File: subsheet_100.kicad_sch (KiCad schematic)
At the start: 21 parts, among them U100 MC68000_PLCC_68_PHY, U100_DIP64 MC68000_DIP_64_SOCKET

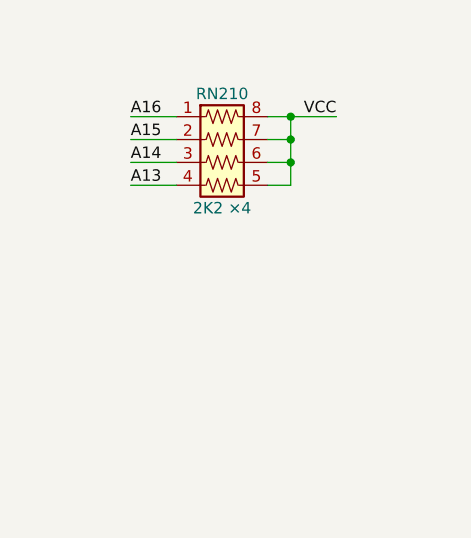
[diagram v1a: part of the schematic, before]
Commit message: add gnd/vcc symbol to start replacing local labels
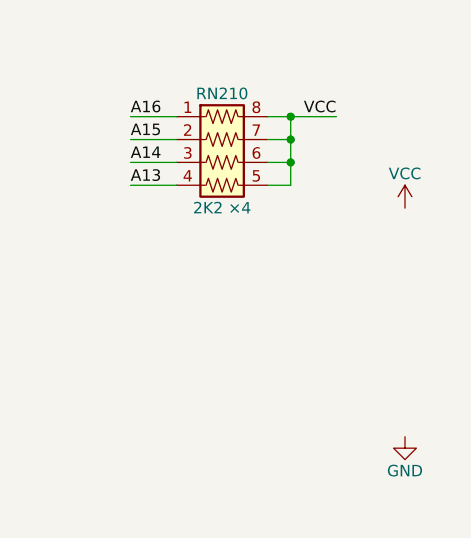
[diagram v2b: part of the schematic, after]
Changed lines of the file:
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@@
     (pin "8")
   )
+  (symbol (lib_id "power:VCC") (at 185.42 214.63 0) (unit 1)
+    (in_bom yes) (on_board yes)
+    (property "Reference" "#PWR?" (id 0) (at 185.42 218.44 0)
+      (effects (font (size 1.27 1.27)) hide)
+    )
+    (property "Value" "VCC" (id 1) (at 185.42 210.82 0))
+    (property "Footprint" "" (id 2) (at 185.42 214.63 0)
+      (effects (font (size 1.27 1.27)) hide)
+    )
+    (property "Datasheet" "" (id 3) (at 185.42 214.63 0)
+      (effects (font (size 1.27 1.27)) hide)
+    )
+    (pin "1")
+  )
+  (symbol (lib_id "power:GND") (at 185.42 240.03 0) (unit 1)
+    (in_bom yes) (on_board yes)
+    (property "Reference" "#PWR?" (id 0) (at 185.42 246.38 0)
+      (effects (font (size 1.27 1.27)) hide)
+    )
+    (property "Value" "GND" (id 1) (at 185.42 243.84 0))
+    (property "Footprint" "" (id 2) (at 185.42 240.03 0)
+      (effects (font (size 1.27 1.27)) hide)
+    )
+    (property "Datasheet" "" (id 3) (at 185.42 240.03 0)
+      (effects (font (size 1.27 1.27)) hide)
+    )
+    (pin "1")
+  )
 )
